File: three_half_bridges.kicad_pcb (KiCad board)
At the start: 4 copper layers, 100 x 100 mm, 164 parts, among them J1 Conn_01x06_Pin, J10 Conn_01x02_Pin, J2 Conn_01x06_Pin, J3 Conn_01x06_Pin, J4 Current Sense, J5 Conn_01x01_Socket, J6 Conn_01x01_Socket, J7 Conn_01x01_Socket, J8 Conn_01x01_Socket, J9 Conn_01x01_Socket, Q3 Q_NIGBT_GCE, Q4 Q_NIGBT_GCE, Q5 Q_NIGBT_GCE, Q6 Q_NIGBT_GCE, Q7 Q_NIGBT_GCE, Q8 Q_NIGBT_GCE, U1 ACS730xLCTR-50AB, U10 ADuM121N, U11 SO8 GATE DRVR, U12 SO8 GATE DRVR, U13 SO8 GATE DRVR, U14 SO8 GATE DRVR, U15 SO8 GATE DRVR, U17 ACS730xLCTR-50AB, U18 ADuM121N, U19 ADuM121N, U2 ACS730xLCTR-50AB, U22 SO8 GATE DRVR, U3 SN6505BDBV, U4 ADuM121N, U5 ADuM121N, U6 SN6505BDBV, U7 SN6505BDBV, U8 SN6505BDBV, U9 ADuM121N

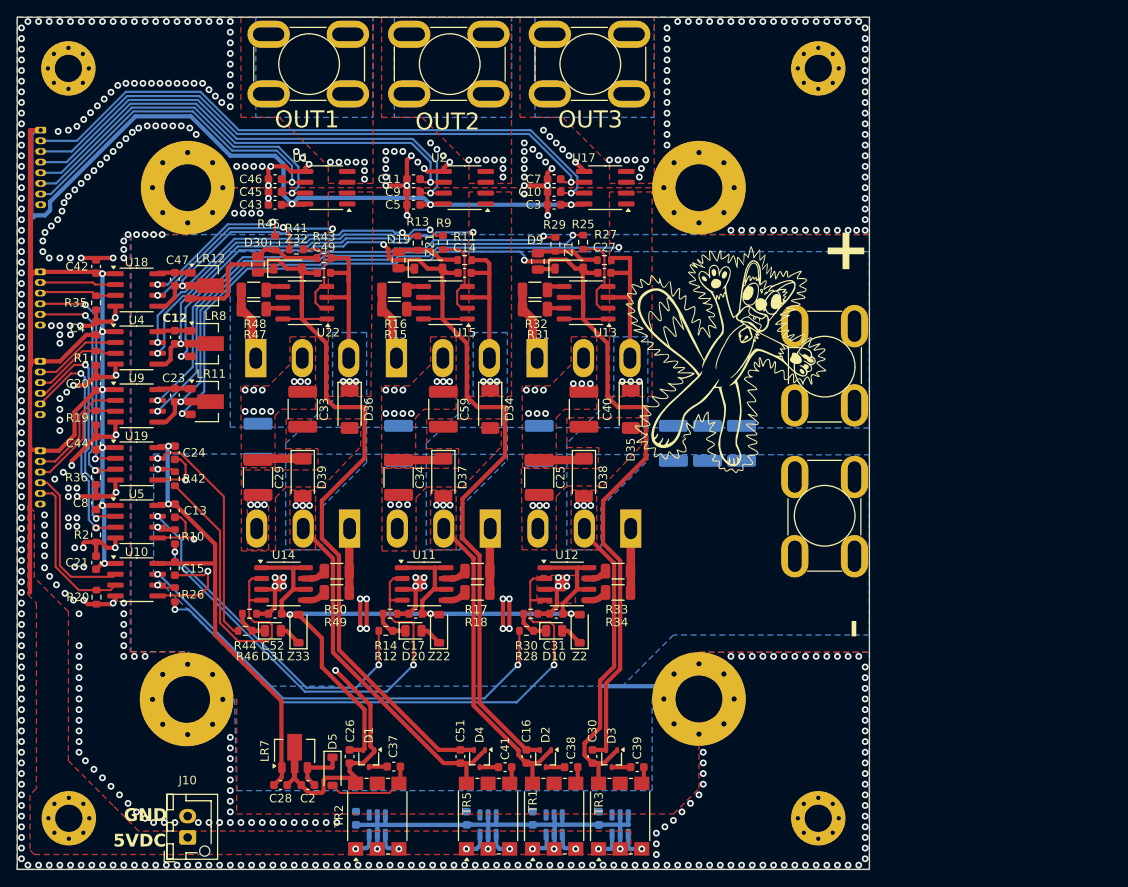
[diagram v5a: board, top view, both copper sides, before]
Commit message: fixed many issues from previous itteration, added design rule checks to enforce minumum 2mm clearence between LV and HV side
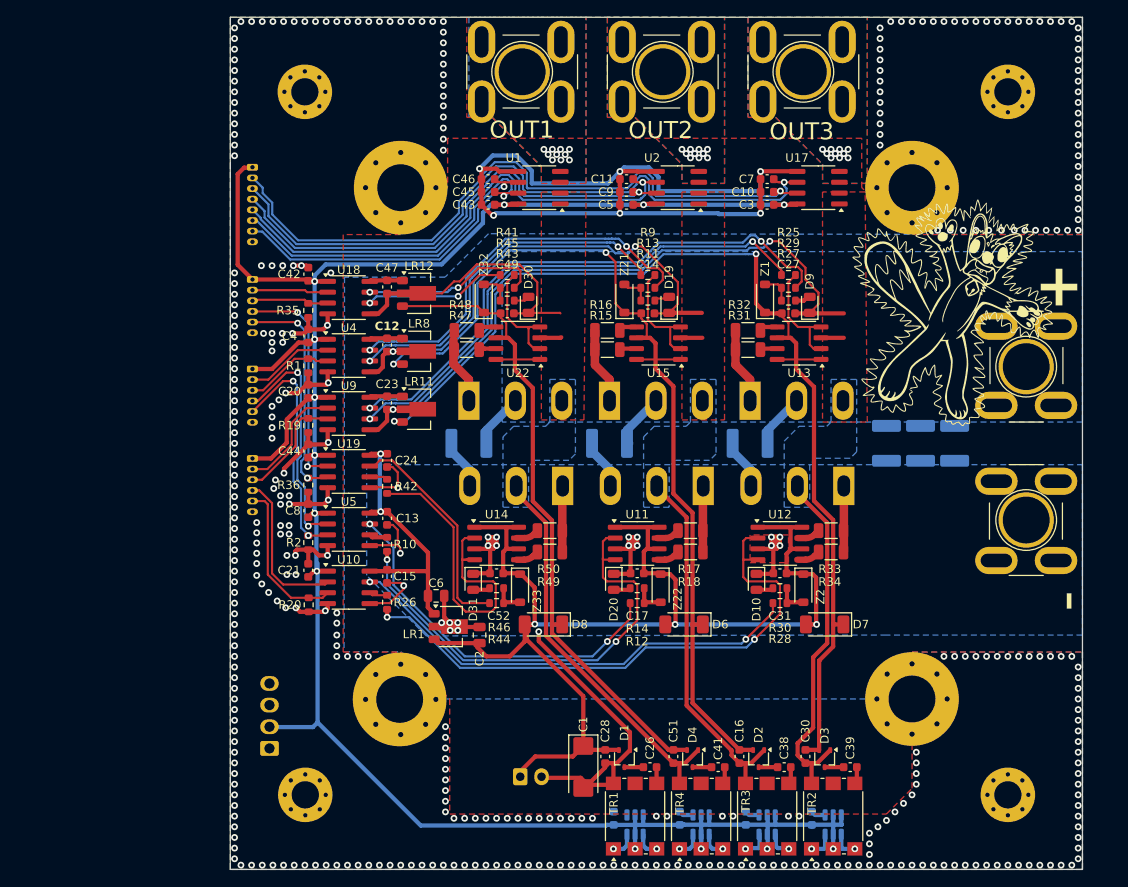
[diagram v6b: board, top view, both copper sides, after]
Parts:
- removed C29, C33, C34, C40, C59: 470n, Capacitor_SMD:C_1812_4532Metric
- removed C37: 1u, Capacitor_SMD:C_0603_1608Metric
- removed D34, D35, D36, D37, D38, D39: FAST 1A DIODE, Diode_SMD:D_SOD-128
- removed D5: D_Schottky, Diode_SMD:D_SOD-123
- removed LR7: MC78L08_SOT89, Package_TO_SOT_SMD:SOT-89-3
- removed the TR2 at (122.2, 123.8)
- added C6: 1u, Capacitor_SMD:C_0805_2012Metric, F.Cu at (129.2, 97.9)
- added D6: FAST 1A DIODE, Diode_SMD:D_SOD-128, F.Cu at (158.2, 101.2)
- added D7: FAST 1A DIODE, Diode_SMD:D_SOD-128, F.Cu at (174.8, 101.2)
- added D8: FAST 1A DIODE, Diode_SMD:D_SOD-128, F.Cu at (141.8, 101.2)
- added LR1: MC78L05_SOT89, Package_TO_SOT_SMD:SOT-89-3, F.Cu at (130.9, 101.5)
- added M1: Fan_4pin, Connector_Molex:Molex_KK-254_AE-6410-04A_1x04_P2.54mm_Vertical, B.Cu at (109.6, 115.8)
- added TR1: EPC3668G, Transformer_SMD:Pulse_PA2004NL, F.Cu at (152.5, 123.8)
- C1: value 1u -> C_Polarized; footprint Capacitor_SMD:C_0603_1608Metric -> Capacitor_Tantalum_SMD:CP_EIA-6032-20_AVX-F; moved to F.Cu
- C12, C13, C15, C23, C24, C47: value 100n -> 1u
- C2: value 1u -> 100n; footprint Capacitor_SMD:C_0603_1608Metric -> Capacitor_SMD:C_0805_2012Metric
- C25: value 470n -> 1u; footprint Capacitor_SMD:C_1812_4532Metric -> Capacitor_SMD:C_0603_1608Metric; moved to B.Cu
- D19, D30, D9: footprint Capacitor_SMD:C_0805_2012Metric -> LED_SMD:LED_0805_2012Metric
- J10: footprint Connector_JST:JST_XH_B2B-XH-AM_1x02_P2.50mm_Vertical -> Connector_JST:JST_XH_B2B-XH-A_1x02_P2.50mm_Vertical; moved to B.Cu
- LR11, LR12, LR8: value MC78L08_SOT89 -> MC78L05_SOT89
- R11, R14, R27, R30, R43, R46: value 1k -> 220
- R15, R16, R17, R18, R31, R32, R33, R34, R47, R48, R49, R50: value 5 -> 2.2
- moved C35 41.2 mm to (166.0, 80.0), turned to 0 degrees
- moved C25 40.9 mm to (150.0, 124.0), turned to -90 degrees
- moved J10 39.7 mm to (139.0, 119.1), turned to 0 degrees
- moved C28 38.2 mm to (149.0, 116.8), turned to 90 degrees
- moved C26 35.3 mm to (154.2, 118.0), turned to 180 degrees
- moved D9 32.3 mm to (173.0, 63.8), turned to 90 degrees
- moved D19 32.2 mm to (156.5, 63.8), turned to 90 degrees
- moved D30 32.1 mm to (140.0, 63.8), turned to 90 degrees
- moved U8 30.2 mm to (152.5, 124.8)
- moved D1 30.0 mm to (151.2, 117.0)
- moved R28 29.9 mm to (169.5, 98.8)
- moved R12 29.7 mm to (152.8, 98.8)
- moved R44 29.7 mm to (136.2, 98.8)
- moved R30 29.4 mm to (169.5, 97.0), turned to 180 degrees
- moved R14 29.2 mm to (152.8, 97.0), turned to 180 degrees
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- renumbered TR3 to TR2, TR1 to TR3, TR5 to TR4
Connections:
- C1 pad 1: GND -> 15V_HV
- C1 pad 2: +5V -> -VDC
- C17 pad 2: 12V_HV -> 15V_HV
- C2 pad 2: Net-(D5-K) -> 15V_HV
- C25 pad 1: -VDC -> GND
- C25 pad 2: +VDC -> +5V
- C26 pad 1: 12V_HV -> Net-(C26-Pad1)
- C26 pad 2: -VDC -> Net-(D1-COM)
- C28 pad 1: 5V_HV -> -VDC
- C28 pad 2: -VDC -> 15V_HV
- C31 pad 2: 12V_HV -> 15V_HV
- C52 pad 2: 12V_HV -> 15V_HV
- D1 pad 2: 12V_HV -> 15V_HV
- D10 pad 1: Net-(D10-K) -> -VDC
- D19 pad 1: Net-(D19-K) -> /half bridge 2/SWNODE
- D20 pad 1: Net-(D20-K) -> -VDC
- D30 pad 1: Net-(D30-K) -> /half bridge 3/SWNODE
- D31 pad 1: Net-(D31-K) -> -VDC
- D9 pad 1: Net-(D9-K) -> /half bridge 1/SWNODE
- J10 pad 1: +5V -> 15V_HV
- J10 pad 2: GND -> -VDC
- R11 pad 1: Net-(D19-K) -> Net-(Z21-A)
- R11 pad 2: /half bridge 2/SWNODE -> Net-(D19-A)
- R12 pad 1: Net-(D20-K) -> Net-(Z22-A)
- R13 pad 2: Net-(D19-K) -> Net-(Z21-A)
- R14 pad 1: Net-(D20-K) -> Net-(Z22-A)
- R14 pad 2: -VDC -> Net-(D20-A)
- R27 pad 1: Net-(D9-K) -> Net-(Z1-A)
- R27 pad 2: /half bridge 1/SWNODE -> Net-(D9-A)
- R28 pad 1: Net-(D10-K) -> Net-(Z2-A)
- R29 pad 2: Net-(D9-K) -> Net-(Z1-A)
- R30 pad 1: Net-(D10-K) -> Net-(Z2-A)
- R30 pad 2: -VDC -> Net-(D10-A)
- R43 pad 1: Net-(D30-K) -> Net-(Z32-A)
- R43 pad 2: /half bridge 3/SWNODE -> Net-(D30-A)
- R44 pad 1: Net-(D31-K) -> Net-(Z33-A)
- R45 pad 2: Net-(D30-K) -> Net-(Z32-A)
- R46 pad 1: Net-(D31-K) -> Net-(Z33-A)
- R46 pad 2: -VDC -> Net-(D31-A)
- U11 pad 1: 12V_HV -> 15V_HV
- U11 pad 6: 12V_HV -> 15V_HV
- U11 pad 8: 12V_HV -> 15V_HV
- U12 pad 1: 12V_HV -> 15V_HV
- U12 pad 6: 12V_HV -> 15V_HV
- U12 pad 8: 12V_HV -> 15V_HV
- U14 pad 1: 12V_HV -> 15V_HV
- U14 pad 6: 12V_HV -> 15V_HV
- U14 pad 8: 12V_HV -> 15V_HV
- Z1 pad 1: Net-(D9-A) -> Net-(D3-K)
- Z1 pad 2: Net-(D3-K) -> Net-(Z1-A)
- Z2 pad 1: Net-(D10-A) -> 15V_HV
- Z2 pad 2: 12V_HV -> Net-(Z2-A)
- Z21 pad 1: Net-(D19-A) -> Net-(D2-K)
- Z21 pad 2: Net-(D2-K) -> Net-(Z21-A)
- Z22 pad 1: Net-(D20-A) -> 15V_HV
- Z22 pad 2: 12V_HV -> Net-(Z22-A)
- Z32 pad 1: Net-(D30-A) -> Net-(D4-K)
- Z32 pad 2: Net-(D4-K) -> Net-(Z32-A)
- Z33 pad 1: Net-(D31-A) -> 15V_HV
- Z33 pad 2: 12V_HV -> Net-(Z33-A)
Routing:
- net 15V_HV: track 0.00 -> 146.3 mm, vias 0 -> 3
- net 12V_HV: track 96.7 -> 0.00 mm, vias 3 -> 0
- net GND: track 100.0 -> 161.0 mm, vias 501 -> 380
- net +5V: track 325.1 -> 274.7 mm
- net 5V_HV: track 56.4 -> 32.3 mm
- net Net-(D4-K): track 102.7 -> 82.0 mm
- net Net-(D3-K): track 141.6 -> 128.0 mm
- net Net-(D5-A): track 11.4 -> 0.00 mm
- net -VDC: track 116.3 -> 126.8 mm, vias 33 -> 21
- net Net-(D2-K): track 120.0 -> 109.5 mm
- net /half bridge 1/~{FLT}: track 72.7 -> 81.4 mm
- net Net-(U4-VIA): track 38.3 -> 46.1 mm
- net Net-(D30-K): track 7.67 -> 0.00 mm
- net Net-(D9-K): track 7.64 -> 0.00 mm
- net Net-(D19-K): track 7.61 -> 0.00 mm
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- removed copper zone on F.Cu, net +5V
- removed copper zone on F.Cu, net +VDC
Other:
- board text removed: "5VDC"
- board text removed: "GND"
